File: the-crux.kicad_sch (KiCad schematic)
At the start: 0 parts

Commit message: Wire LEDs
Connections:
- no-connect marks 0 -> 1
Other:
- added sheet LEDs (leds.kicad_sch)
- company: (none) -> Ayo Reis
- title: (none) -> The Crux
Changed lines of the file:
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@@
 	(generator_version "9.0")
 	(paper "A4")
+	(title_block
+		(title "The Crux")
+		(company "Ayo Reis")
+	)
+	(no_connect
+		(at 45.72 27.94)
+	)
+	(wire
+		(pts
+			(xy 44.45 27.94) (xy 45.72 27.94)
+		)
+		(stroke
+			(width 0)
+			(type default)
+		)
+	)
+	(sheet
+		(at 25.4 25.4)
+		(size 19.05 5.08)
+		(exclude_from_sim no)
+		(in_bom yes)
+		(on_board yes)
+		(dnp no)
+		(fields_autoplaced yes)
+		(stroke
+			(width 0.1524)
+			(type solid)
+		)
+		(fill
+			(color 0 0 0 0.0000)
+		)
+		(property "Sheetname" "LEDs"
+			(at 25.4 24.6884 0)
+			(effects
+				(font
+					(size 1.27 1.27)
+				)
+				(justify left bottom)
+			)
+		)
+		(property "Sheetfile" "leds.kicad_sch"
+			(at 25.4 31.0646 0)
+			(effects
+				(font
+					(size 1.27 1.27)
+				)
+				(justify left top)
+			)
+		)
+		(pin "DIN" input
+			(at 44.45 27.94 0)
+			(effects
+				(font
+					(size 1.27 1.27)
+				)
+				(justify right)
+			)
+		)
+		(instances
+			(project "the-crux"
+				(path "/4df6b704-ba7b-4758-9572-31efc60a9341"
+					(page "2")
+				)
+			)
+		)
+	)
 	(sheet_instances
 		(path "/"

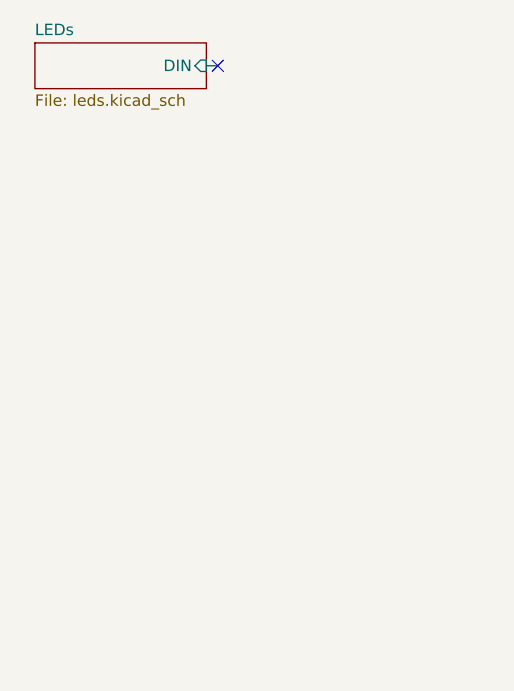
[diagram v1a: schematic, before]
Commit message: Wire linear hall-effect sensors and analog multiplexers
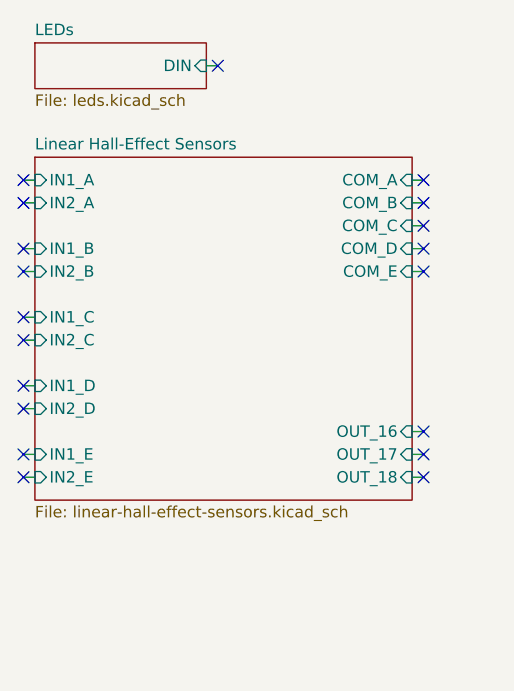
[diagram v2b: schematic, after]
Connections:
- no-connect marks 1 -> 19
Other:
- added sheet Linear Hall-Effect Sensors (linear-hall-effect-sensors.kicad_sch)

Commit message: Wire switches
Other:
- added sheet Switches (switches.kicad_sch)
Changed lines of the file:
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@@
+	)
+	(sheet
+		(at 25.4 88.9)
+		(size 22.86 3.81)
+		(exclude_from_sim no)
+		(in_bom yes)
+		(on_board yes)
+		(dnp no)
+		(fields_autoplaced yes)
+		(stroke
+			(width 0.1524)
+			(type solid)
+		)
+		(fill
+			(color 0 0 0 0.0000)
+		)
+		(property "Sheetname" "Switches"
+			(at 25.4 88.1884 0)
+			(effects
+				(font
+					(size 1.27 1.27)
+				)
+				(justify left bottom)
+			)
+		)
+		(property "Sheetfile" "switches.kicad_sch"
+			(at 25.4 93.2946 0)
+			(effects
+				(font
+					(size 1.27 1.27)
+				)
+				(justify left top)
+			)
+		)
+		(instances
+			(project "the-crux"
+				(path "/4df6b704-ba7b-4758-9572-31efc60a9341"
+					(page "4")
+				)
+			)
+		)
 	)
 	(sheet
